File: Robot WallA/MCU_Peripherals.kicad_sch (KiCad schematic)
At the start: 48 parts, among them IC3 USBLC6-4SC6, IC4 USBLC6-4SC6, J2 USB4216-03-A, J3 SS-90000-009, T1 H1102NL, U7 LAN8742A, Y2 Crystal_GND24

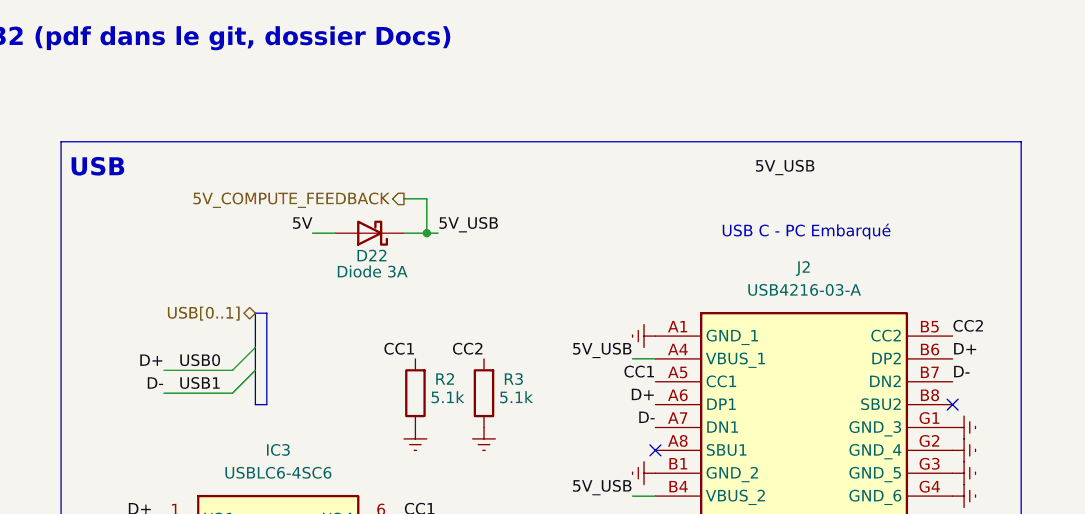
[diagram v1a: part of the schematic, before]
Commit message: Added pin header for 5V USB type output, to be able to disable it
Updated fab files
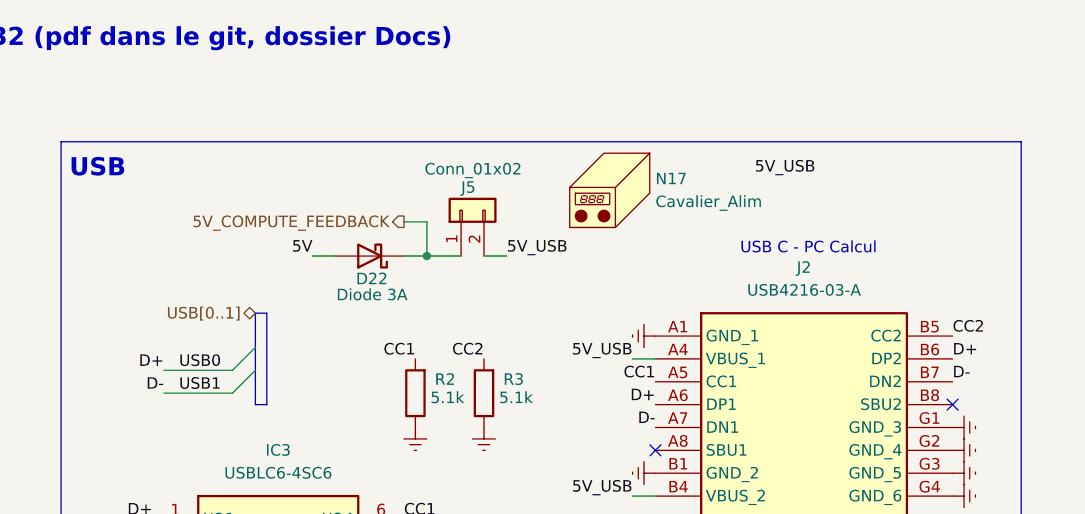
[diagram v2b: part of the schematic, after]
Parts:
- added J5: Conn_01x02, Connector_PinHeader_2.54mm:PinHeader_1x02_P2.54mm_Vertical, symbol Connector_Generic:Conn_01x02
- added N17: Cavalier_Alim, symbol Mechanical:Housing
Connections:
- net 5V_COMPUTE_FEEDBACK: now also J5.1 (Pin_1); no longer IC3.5 (VBUS), J2.A4 (VBUS_1), J2.B4 (VBUS_2)
- new net 5V_USB: IC3.5 (VBUS), J2.A4 (VBUS_1), J2.B4 (VBUS_2), J5.2 (Pin_2)
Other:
- note added: "USB C - PC Calcul"
- note removed: "USB C - PC Embarqué"
- moved on the sheet: D22
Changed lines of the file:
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@@
 		)
 	)
-	(text "USB C - PC Embarqué"
+	(text "USB C - PC Calcul"
 		(exclude_from_sim no)
-		(at 245.364 38.1 0)
+		(at 245.618 39.878 0)
 		(effects
 			(font
@@
 	)
 	(junction
-		(at 203.2 38.1)
+		(at 203.2 40.64)
 		(diameter 0)
 		(color 0 0 0 0)
@@
 	(wire
 		(pts
-			(xy 203.2 38.1) (xy 200.66 38.1)
+			(xy 203.2 40.64) (xy 200.66 40.64)
 		)
 		(stroke
@@
 	(wire
 		(pts
-			(xy 204.47 38.1) (xy 203.2 38.1)
+			(xy 207.01 40.64) (xy 203.2 40.64)
 		)
 		(stroke
@@
 		)
 	)
+	(wire
+		(pts
+			(xy 212.09 40.64) (xy 209.55 40.64)
+		)
+		(stroke
+			(width 0)
+			(type default)
+		)
+	)
 	(bus
 		(pts
@@
 	(wire
 		(pts
-			(xy 203.2 34.29) (xy 203.2 38.1)
+			(xy 203.2 36.83) (xy 203.2 40.64)
 		)
 		(stroke
@@
 	(wire
 		(pts
-			(xy 193.04 38.1) (xy 190.5 38.1)
+			(xy 193.04 40.64) (xy 190.5 40.64)
 		)
 		(stroke
@@
 	(wire
 		(pts
-			(xy 200.66 34.29) (xy 203.2 34.29)
+			(xy 200.66 36.83) (xy 203.2 36.83)
 		)
 		(stroke
@@
 	)
 	(label "5V"
-		(at 190.5 38.1 180)
+		(at 190.5 40.64 180)
 		(effects
 			(font
@@
 	)
 	(label "5V_USB"
-		(at 204.47 38.1 0)
+		(at 212.09 40.64 0)
 		(effects
 			(font
@@
 	(hierarchical_label "5V_COMPUTE_FEEDBACK"
 		(shape output)
-		(at 200.66 34.29 180)
+		(at 200.66 36.83 180)
 		(effects
 			(font
@@
 	(symbol
 		(lib_id "Diode:SB120")
-		(at 196.85 38.1 180)
+		(at 196.85 40.64 180)
 		(unit 1)
 		(exclude_from_sim no)
@@
 		(dnp no)
 		(property "Reference" "D22"
-			(at 197.104 40.64 0)
+			(at 197.104 43.18 0)
 			(effects
 				(font
@@
 		)
 		(property "Value" "Diode 3A"
-			(at 197.104 42.418 0)
+			(at 197.104 44.958 0)
 			(effects
 				(font
@@
 		)
 		(property "Footprint" "Diode_SMD:D_SMP_DO-220AA"
-			(at 196.85 33.655 0)
+			(at 196.85 36.195 0)
 			(effects
 				(font
@@
 		)
 		(property "Datasheet" ""
-			(at 196.85 38.1 0)
+			(at 196.85 40.64 0)
 			(effects
 				(font
@@
 		)
 		(property "Description" ""
-			(at 196.85 38.1 0)
+			(at 196.85 40.64 0)
 			(effects
 				(font
@@
 		)
 		(property "Manufacturer_Part_Number" "SS3P4-M3/84A"
-			(at 196.85 38.1 0)
+			(at 196.85 40.64 0)
 			(effects
 				(font
@@
 	)
 	(symbol
+		(lib_id "Mechanical:Housing")
+		(at 224.79 33.02 0)
+		(unit 1)
+		(exclude_from_sim no)
+		(in_bom yes)
+		(on_board no)
+		(dnp no)
+		(property "Reference" "N17"
+			(at 228.6 32.0674 0)
+			(effects
+				(font
+					(size 1.27 1.27)
+				)
+				(justify left)
+			)
+		)
+		(property "Value" "Cavalier_Alim"
+			(at 228.6 34.6074 0)
+			(effects
+				(font
+					(size 1.27 1.27)
+				)
+				(justify left)
+			)
+		)
+		(property "Footprint" ""
+			(at 226.06 31.75 0)
+			(effects
+				(font
+					(size 1.27 1.27)
+				)
+				(hide yes)
+			)
+		)
+		(property "Datasheet" "~"
+			(at 226.06 31.75 0)
+			(effects
+				(font
+					(size 1.27 1.27)
+				)
+				(hide yes)
+			)
+		)
+		(property "Description" "Housing"
+			(at 224.79 33.02 0)
+			(effects
+				(font
+					(size 1.27 1.27)
+				)
+				(hide yes)
+			)
+		)
+		(property "Manufacturer_Part_Number" "15-29-1024"
+			(at 224.79 33.02 0)
+			(effects
+				(font
+					(size 1.27 1.27)
+				)
+				(hide yes)
+			)
+		)
+		(instances
+			(project "Robot WallA"
+				(path "/117fd49e-499d-4b54-b58c-f6b538ecca4a/b9176f6a-4299-4bca-a59b-5ff3df09c616/6ae8cb66-0d01-49c6-940e-175426e825e5"
+					(reference "N17")
+					(unit 1)
+				)
+			)
+		)
+	)
+	(symbol
 		(lib_id "Device:R")
 		(at 209.55 55.88 180)
@@
 					(unit 1)
 				)
+			)
+		)
+	)
+	(symbol
+		(lib_id "Connector_Generic:Conn_01x02")
+		(at 207.01 35.56 90)
+		(unit 1)
+		(exclude_from_sim no)
+		(in_bom yes)
+		(on_board yes)
+		(dnp no)
+		(property "Reference" "J5"
+			(at 207.01 33.02 90)
+			(effects
+				(font
+					(size 1.27 1.27)
+				)
+				(justify right)
+			)
+		)
+		(property "Value" "Conn_01x02"
+			(at 202.946 30.988 90)
+			(effects
+				(font
+					(size 1.27 1.27)
+				)
+				(justify right)
+			)
+		)
+		(property "Footprint" "Connector_PinHeader_2.54mm:PinHeader_1x02_P2.54mm_Vertical"
+			(at 207.01 35.56 0)
+			(effects
+				(font
+					(size 1.27 1.27)
+				)
+				(hide yes)
+			)
+		)
+		(property "Datasheet" "~"
+			(at 207.01 35.56 0)
+			(effects
+				(font
+					(size 1.27 1.27)
+				)
+				(hide yes)
+			)
+		)
+		(property "Description" "Generic connector, single row, 01x02, script generated (kicad-library-utils/schlib/autogen/connector/)"
+			(at 207.01 35.56 0)
+			(effects
+				(font
+					(size 1.27 1.27)
+				)
+				(hide yes)
+			)
+		)
+		(pin "1"
+		)
+		(pin "2"
+		)
+		(instances
+			(project "Robot WallA"
+				(path "/117fd49e-499d-4b54-b58c-f6b538ecca4a/b9176f6a-4299-4bca-a59b-5ff3df09c616/6ae8cb66-0d01-49c6-940e-175426e825e5"
+					(reference "J5")
+					(unit 1)
+				)

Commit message: Modified footprint to simplify BOM. Finalized BOM.
Updated fab files
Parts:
- C115: Manufacturer_Part_Number (none) -> C0603C471K5RACTU
- C116, C24, C25, C26, C29, C30: Manufacturer_Part_Number (none) -> KGM15BR71H104KT
- C32: value 1uF -> 1uF/50V; Manufacturer_Part_Number (none) -> CL10A105KB8NNNC
- J5, JP4: now left out of the parts list
- R10, R13, R20, R8, R9: footprint Resistor_SMD:R_0603_1608Metric -> Resistor_SMD:R_0603_1608Metric_Pad0.98x0.95mm_HandSolder; Manufacturer_Part_Number (none) -> 667-ERJ-3GEYJ103V
- R11, R12, R14, R18: footprint Resistor_SMD:R_0603_1608Metric -> Resistor_SMD:R_0603_1608Metric_Pad0.98x0.95mm_HandSolder; Manufacturer_Part_Number (none) -> CRCW060333R0JNEA
- R15, R17: footprint Resistor_SMD:R_0603_1608Metric -> Resistor_SMD:R_0603_1608Metric_Pad0.98x0.95mm_HandSolder; Manufacturer_Part_Number (none) -> RC0603JR-071K5L
- R16: footprint Resistor_SMD:R_0603_1608Metric -> Resistor_SMD:R_0603_1608Metric_Pad0.98x0.95mm_HandSolder; Manufacturer_Part_Number (none) -> ERJ-3EKF1212V
- R19, R21: footprint Resistor_SMD:R_0603_1608Metric -> Resistor_SMD:R_0603_1608Metric_Pad0.98x0.95mm_HandSolder; Manufacturer_Part_Number (none) -> RE0603FRE07270RL
- R2, R3: Manufacturer_Part_Number (none) -> CRCW06035K10FKEA
- R22, R23, R24, R25: footprint Resistor_SMD:R_0603_1608Metric -> Resistor_SMD:R_0603_1608Metric_Pad0.98x0.95mm_HandSolder; Manufacturer_Part_Number (none) -> CRCW060375R0FKEAC
- R4, R5, R6, R7: Manufacturer_Part_Number (none) -> CRCW060350R0FKTA
- U7: Manufacturer_Part_Number (none) -> LAN8742A-CZ

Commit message: Added logo
Replaced out of stock components
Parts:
- C23: Manufacturer_Part_Number CC1206KKX7RDBB102 -> CL31A106KQHNNNE
- C31: Manufacturer_Part_Number CC1206KKX7RDBB102 -> 1206B102K102CT
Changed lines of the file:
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@@
 			)
 		)
-		(property "Manufacturer_Part_Number" "CC1206KKX7RDBB102"
+		(property "Manufacturer_Part_Number" "CL31A106KQHNNNE"
 			(at 102.87 44.45 0)
 			(effects
@@
 			)
 		)
-		(property "Manufacturer_Part_Number" "CC1206KKX7RDBB102"
+		(property "Manufacturer_Part_Number" "1206B102K102CT"
 			(at 799.39 142.24 0)
 			(effects
